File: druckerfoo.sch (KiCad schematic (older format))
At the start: 8 parts

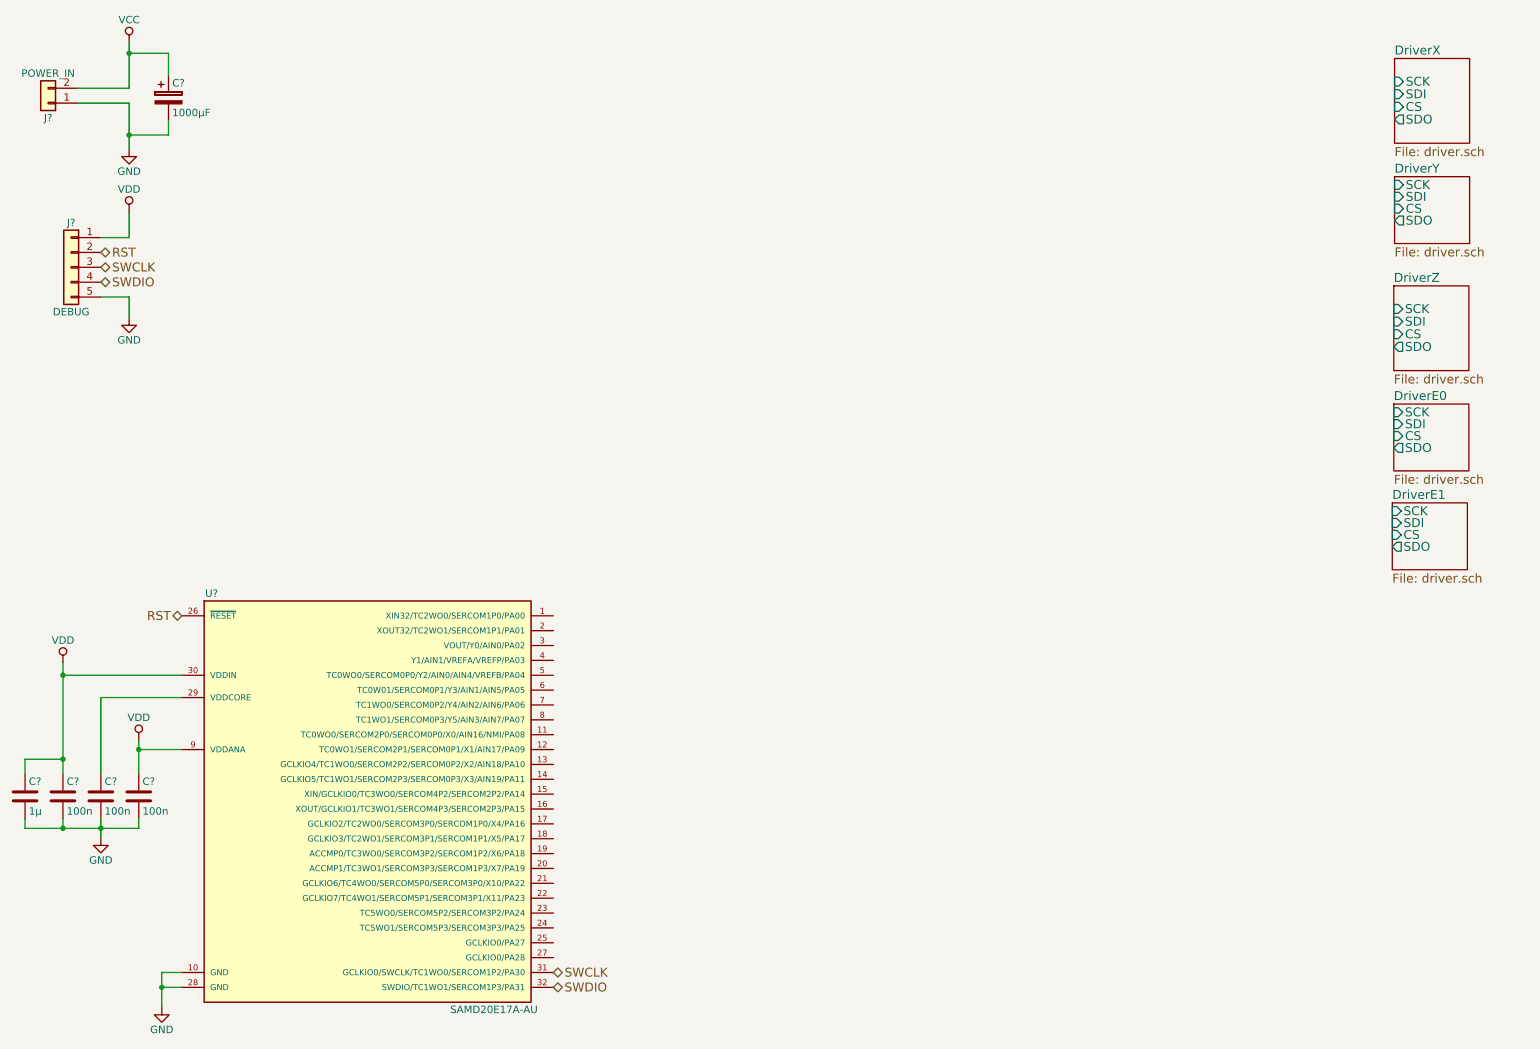
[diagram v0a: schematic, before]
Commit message: Add buck converter for controller
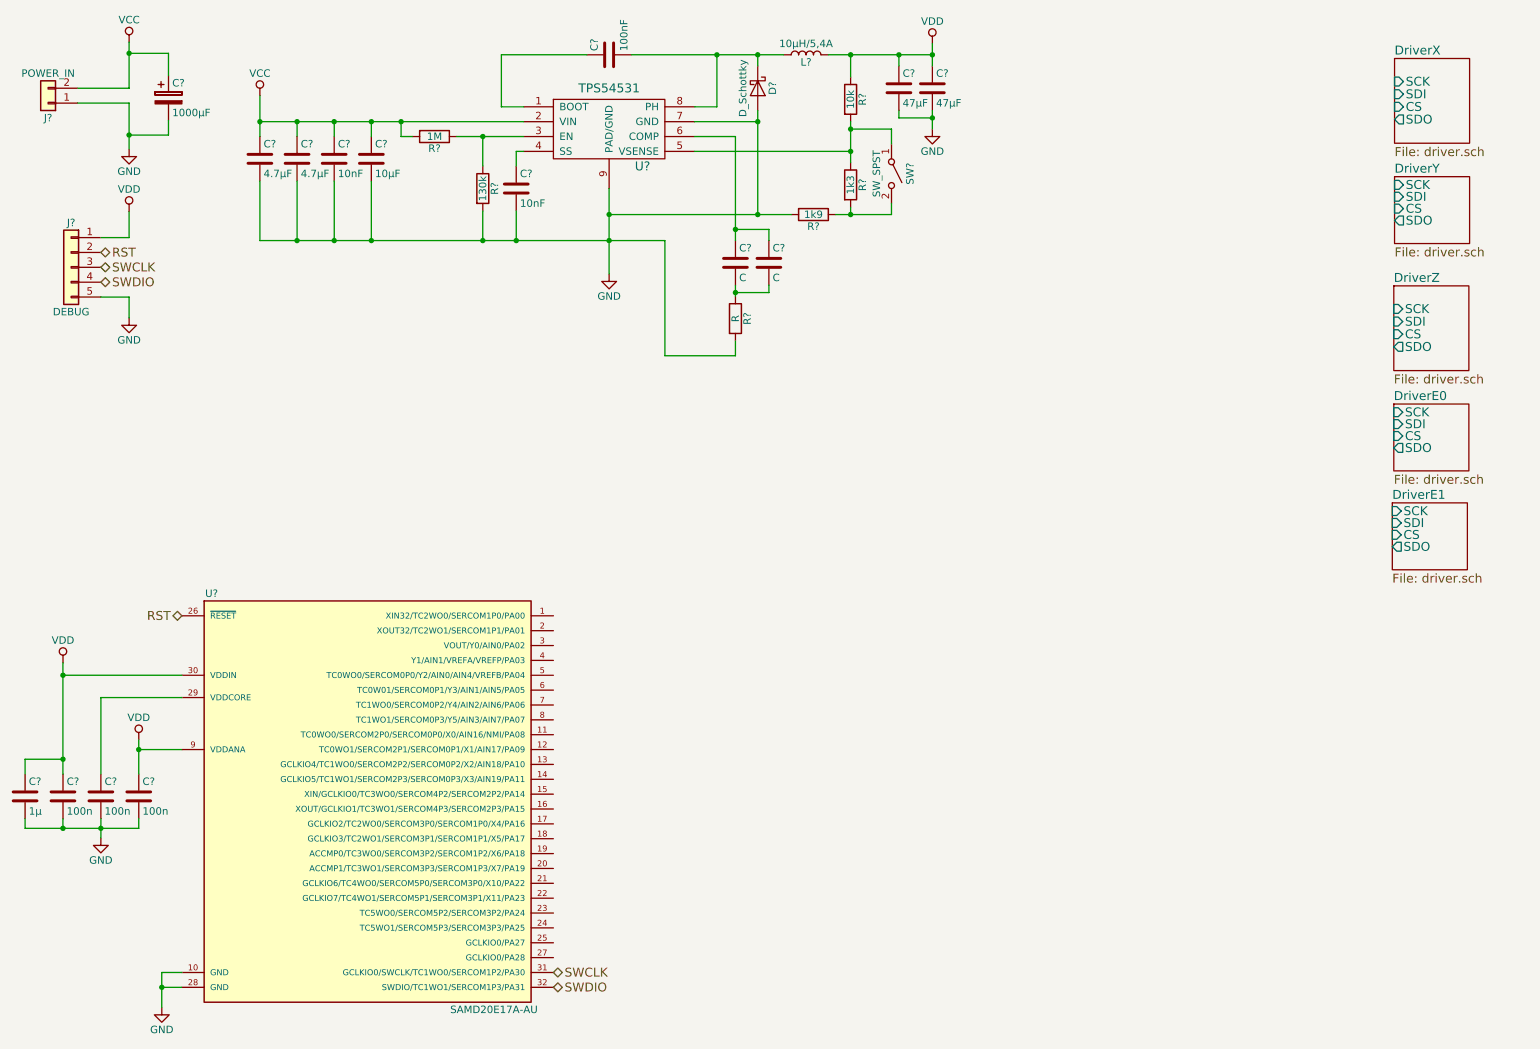
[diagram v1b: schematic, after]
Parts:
- added C? (x2): 10nF, symbol C
- added C?: 100nF, symbol C
- added C? (x2): C, symbol C
- added C? (x2): 47µF, symbol C
- added C?: 10µF, symbol C
- added C? (x2): 4.7µF, symbol C
- added D?: D_Schottky, symbol D_Schottky
- added L?: 10µH/5,4A, symbol L
- added R?: 1M, symbol R
- added R?: 130k, symbol R
- added R?: 10k, symbol R
- added R?: 1k3, symbol R
- added R?: 1k9, symbol R
- added R?: R, symbol R
- added SW?: SW_SPST, symbol SW_SPST
- added U?: TPS54531, symbol TPS54531
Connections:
- net GND: now also C?.2, C?.2, C?.2, C?.2, C?.2, C?.2, C?.2, D?.2 (A), R?.2, R?.2, R?.2, U?.7 (GND), U?.9 (PAD/GND)
- net VCC: now also C?.1, C?.1, C?.1, C?.1, R?.2, U?.2 (VIN)
- net VDD: now also C?.1, C?.1, L?.2, R?.1
- new net: C?.1, U?.1 (BOOT)
- new net: R?.1, R?.1, U?.3 (EN)
- new net: C?.1, U?.4 (SS)
- new net: R?.1, R?.2, SW?.1 (A), U?.5 (VSENSE)
- new net: C?.1, C?.1, U?.6 (COMP)
- new net: C?.2, D?.1 (K), L?.1, U?.8 (PH)
- new net: R?.1, R?.2, SW?.2 (B)
- new net: C?.2, C?.2, R?.1
